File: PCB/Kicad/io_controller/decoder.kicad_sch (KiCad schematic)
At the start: 3 parts, among them U10 74LS08, U11 74LS08, U9 74LS02

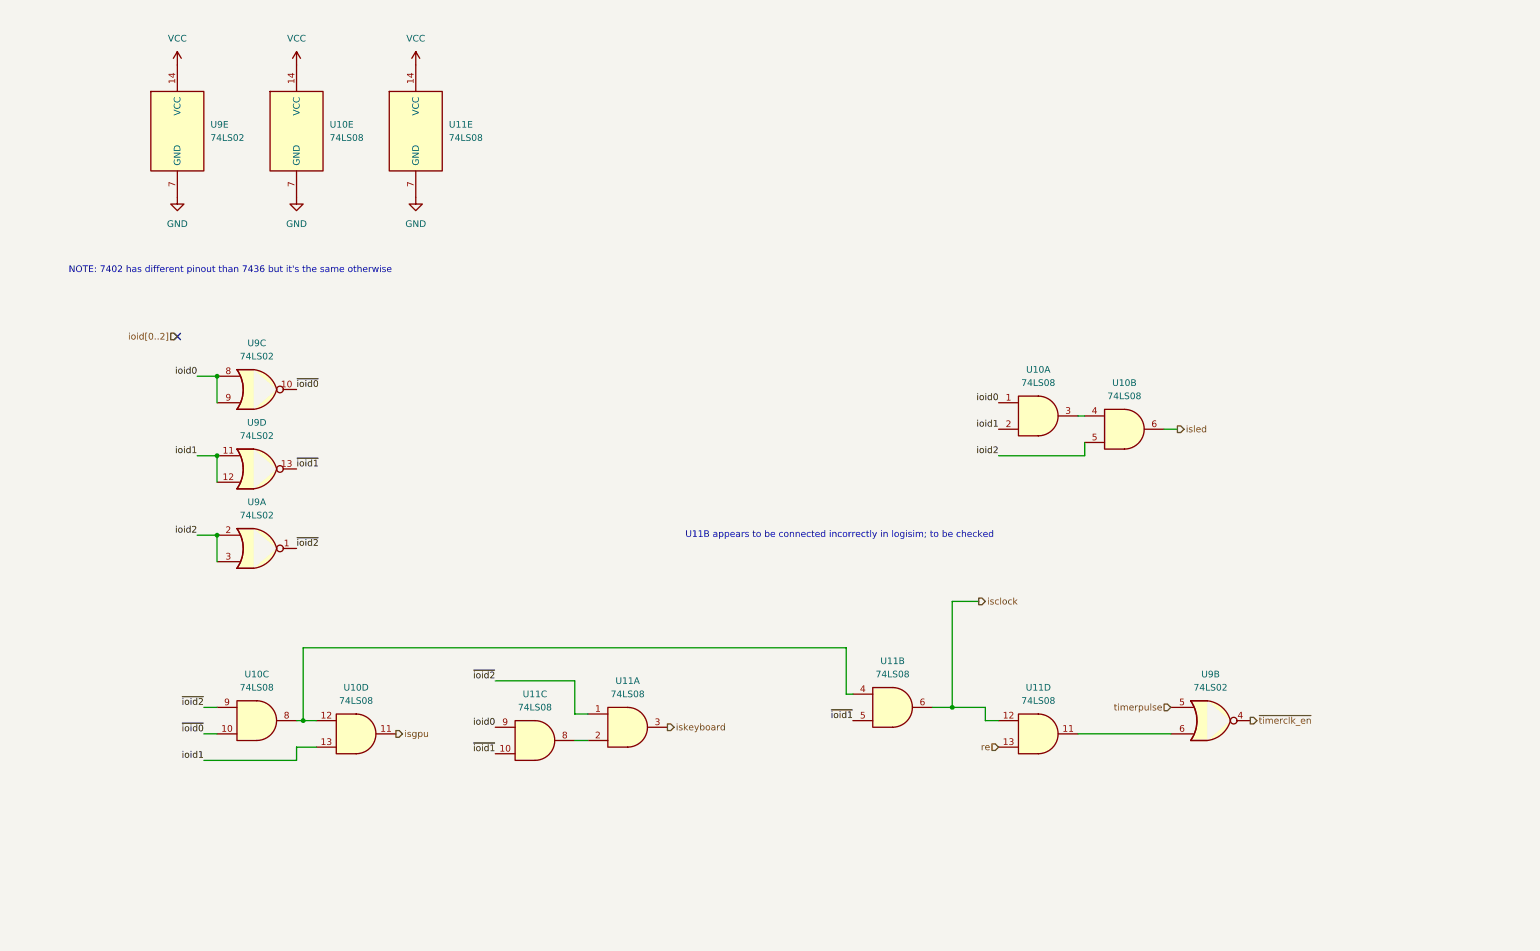
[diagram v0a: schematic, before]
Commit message: initial version of io controller schematic
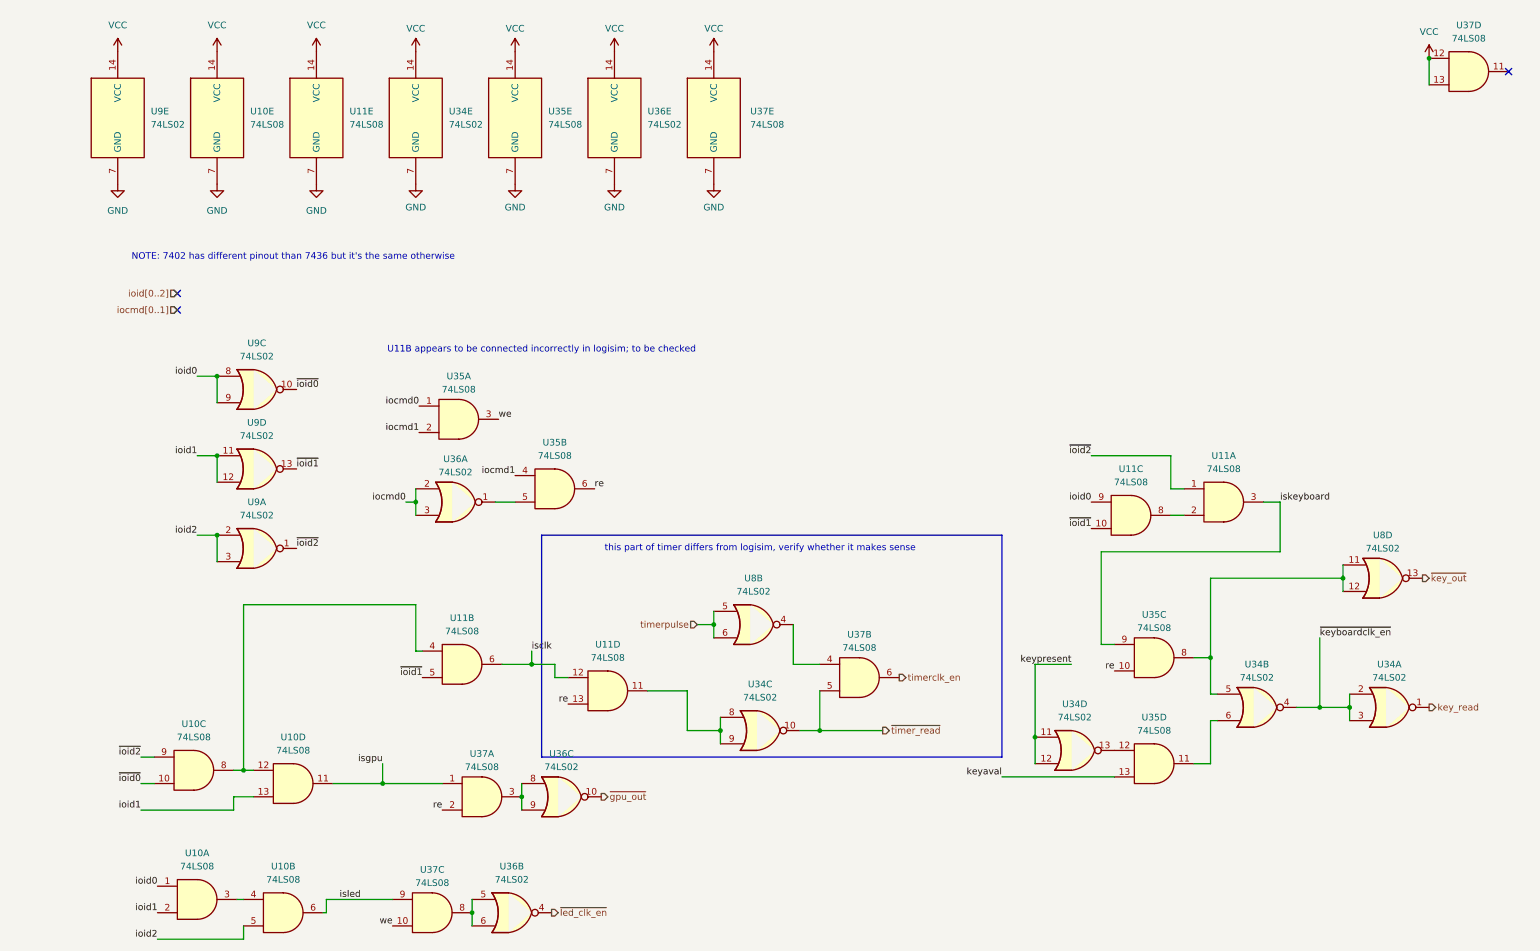
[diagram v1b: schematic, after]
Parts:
- removed unit 2 of U9
- added U34, U36, U8: 74LS02, symbol 74xx:74LS02
- added U35, U37: 74LS08, symbol 74xx:74LS08
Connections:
- net GND: now also U34.7 (GND), U35.7 (GND), U36.7 (GND), U37.7 (GND)
- net VCC: now also U34.14 (VCC), U35.14 (VCC), U36.14 (VCC), U37.12, U37.13, U37.14 (VCC)
- net isgpu: now also U37.1
- net iskeyboard: now also U35.9
- net isled: now also U37.9
- net re: now also U35.10, U35.6, U37.2
- net timerpulse: now also U8.5, U8.6
- net at U11.11: now also U34.8, U34.9
- net isclock renamed isclk
- new net: U37.4, U8.4
- new net: U36.8, U36.9, U37.3
- new net: U35.5, U36.1
- new net: U34.5, U35.8, U8.11, U8.12
- new net: U34.6, U35.11
- new net: U34.13, U35.12
- new net: U36.5, U36.6, U37.8
- new net iocmd0: U35.1, U36.2, U36.3
- new net iocmd1: U35.2, U35.4
- new net key_read: U34.1
- new net keyaval: U35.13
- new net keypresent: U34.11, U34.12
- new net timerclk_en: U37.6
- new net we: U35.3, U37.10
- new net ~{gpu_out}: U36.10
- new net ~{key_out}: U8.13
- new net ~{keyboardclk_en}: U34.2, U34.3, U34.4
- new net ~{led_clk_en}: U36.4
- new net ~{timer_read}: U34.10, U37.5
- no-connect marks 1 -> 3
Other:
- note added: "this part of timer differs from logisim, verify whether it makes sense"
- moved on the sheet: U10A, U10B, U10C, U10D, U10E, U11A, U11B, U11C, U11D, U11E, U9E

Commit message: io controller WIP ; simulated timer ; adjusted decoder ; adjusted LEDs
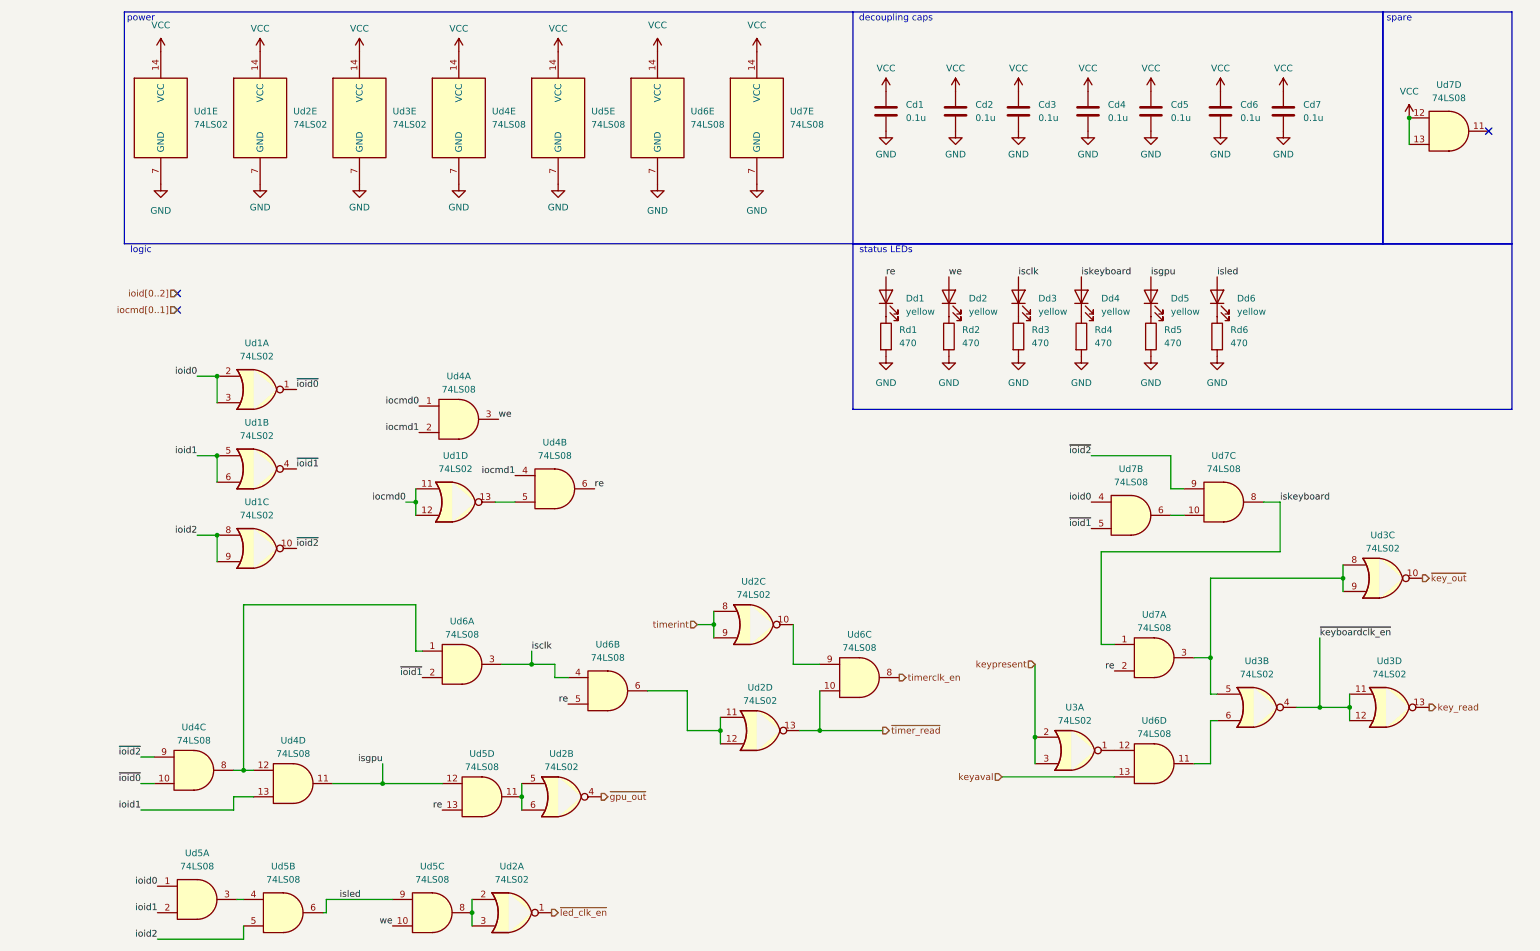
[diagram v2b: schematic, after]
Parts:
- added Cd1, Cd2, Cd3, Cd4, Cd5, Cd6, Cd7: 0.1u, Capacitor_SMD:C_0402_1005Metric, symbol Device:C
- added Dd1, Dd2, Dd3, Dd4, Dd5, Dd6: yellow, LED_SMD:LED_0603_1608Metric, symbol Device:LED
- added Rd1, Rd2, Rd3, Rd4, Rd5, Rd6: 470, Resistor_SMD:R_0402_1005Metric, symbol Device:R
- Ud1: renamed from U9; footprint (none) -> Package_SO:SO-14_3.9x8.65mm_P1.27mm
- Ud1, Ud2, Ud3: renamed from U36; footprint (none) -> Package_SO:SO-14_3.9x8.65mm_P1.27mm
- Ud2, Ud3: renamed from U34; footprint (none) -> Package_SO:SO-14_3.9x8.65mm_P1.27mm
- Ud2, Ud3: renamed from U8; footprint (none) -> Package_SO:SO-14_3.9x8.65mm_P1.27mm
- Ud4, Ud5, Ud6: renamed from U10; footprint (none) -> Package_SO:SOIC-14_3.9x8.7mm_P1.27mm
- Ud4, Ud6, Ud7: renamed from U35; footprint (none) -> Package_SO:SOIC-14_3.9x8.7mm_P1.27mm
- Ud5, Ud6, Ud7: renamed from U37; footprint (none) -> Package_SO:SOIC-14_3.9x8.7mm_P1.27mm
- Ud6, Ud7: renamed from U11; footprint (none) -> Package_SO:SOIC-14_3.9x8.7mm_P1.27mm
- renumbered U34 to U3
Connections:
- net GND: now also Cd1.2, Cd2.2, Cd3.2, Cd4.2, Cd5.2, Cd6.2, Cd7.2, Rd1.2, Rd2.2, Rd3.2, Rd4.2, Rd5.2, Rd6.2
- net VCC: now also Cd1.1, Cd2.1, Cd3.1, Cd4.1, Cd5.1, Cd6.1, Cd7.1
- net iocmd0: now also Ud1.11, Ud1.12; no longer Ud1.2, Ud1.3
- net ioid0: now also Ud1.2, Ud1.3, Ud7.4; no longer Ud1.8, Ud1.9, Ud7.9
- net ioid1: now also Ud1.5, Ud1.6; no longer Ud1.11, Ud1.12
- net ioid2: now also Ud1.8, Ud1.9; no longer Ud1.2, Ud1.3
- net isclk: now also Ud6.3, Ud6.4, Dd3.2 (A); no longer Ud6.12, Ud6.6
- net isgpu: now also Ud5.12, Dd5.2 (A); no longer Ud5.1
- net iskeyboard: now also Ud7.1, Ud7.8, Dd4.2 (A); no longer Ud7.3, Ud7.9
- net isled: now also Dd6.2 (A)
- net key_read: now also Ud3.13; no longer Ud3.1
- net keypresent: now also U3.2, U3.3; no longer U3.11, U3.12
- net re: now also Ud5.13, Ud6.5, Ud7.2, Dd1.2 (A); no longer Ud5.2, Ud6.13, Ud7.10
- net timerclk_en: now also Ud6.8; no longer Ud6.6
- net we: now also Dd2.2 (A)
- net ~{gpu_out}: now also Ud2.4; no longer Ud2.10
- net ~{ioid0}: now also Ud1.1; no longer Ud1.10
- net ~{ioid1}: now also Ud1.4, Ud6.2, Ud7.5; no longer Ud1.13, Ud6.5, Ud7.10
- net ~{ioid2}: now also Ud1.10, Ud7.9; no longer Ud1.1, Ud7.1
- net ~{key_out}: now also Ud3.10; no longer Ud3.13
- net ~{keyboardclk_en}: now also Ud3.11, Ud3.12; no longer Ud3.2, Ud3.3
- net ~{led_clk_en}: now also Ud2.1; no longer Ud2.4
- net ~{timer_read}: now also Ud2.13, Ud6.10; no longer Ud2.10, Ud6.5
- net at Ud4.12, Ud4.8: now also Ud6.1; no longer Ud6.4
- net at Ud4.5: now also Ud1.13; no longer Ud1.1
- net at Ud6.12: now also U3.1; no longer U3.13
- removed net timerpulse: Ud2.5, Ud2.6
- new net: Ud2.10, Ud6.9
- new net: Dd3.1 (K), Rd3.1
- new net: Ud2.5, Ud2.6, Ud5.11
- new net: Ud2.11, Ud2.12, Ud6.6
- new net: Dd2.1 (K), Rd2.1
- new net: Dd5.1 (K), Rd5.1
- new net: Ud3.5, Ud3.8, Ud3.9, Ud7.3
- new net: Ud7.10, Ud7.6
- new net: Dd6.1 (K), Rd6.1
- new net: Ud2.2, Ud2.3, Ud5.8
- new net: Dd4.1 (K), Rd4.1
- new net: Dd1.1 (K), Rd1.1
- new net timerint: Ud2.8, Ud2.9
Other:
- note added: "decoupling caps"
- note added: "logic"
- note added: "power"
- note added: "spare"
- note added: "status LEDs"
- note removed: "NOTE: 7402 has different pinout than 7436 but it's the same otherwise"
- note removed: "U11B appears to be connected incorrectly in logisim; to be checked"
- note removed: "this part of timer differs from logisim, verify whether it makes sense"
- company: (none) -> AGH Logic Unit
- title: (none) -> Decoder
- moved on the sheet: Ud1E, Ud2E, Ud3E, Ud4E, Ud5E, Ud6E, Ud7D, Ud7E

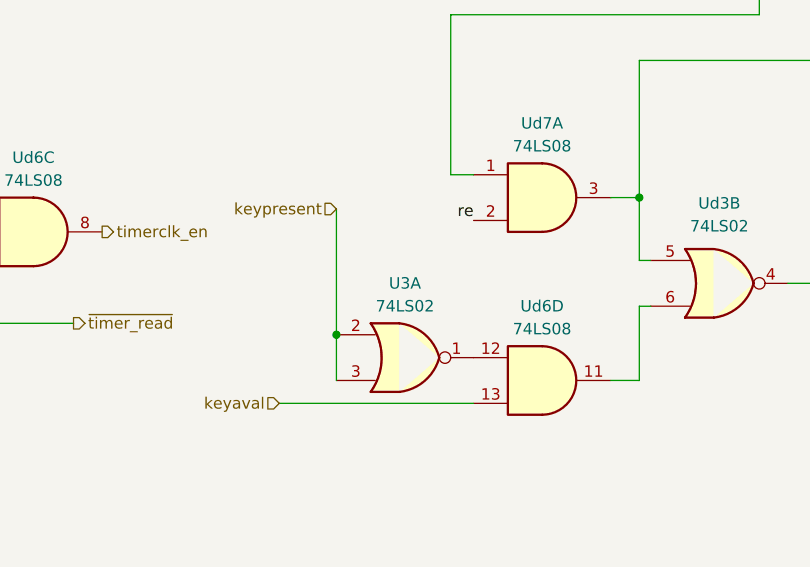
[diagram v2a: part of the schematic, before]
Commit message: more spice models and bugfixes ; more tests of io_controller - mostly keyboard
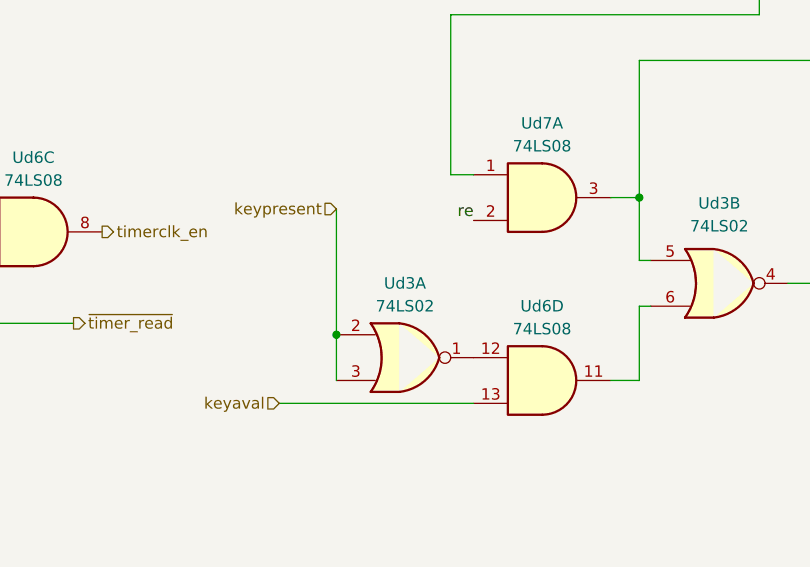
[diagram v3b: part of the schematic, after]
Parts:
- renumbered U3 to Ud3
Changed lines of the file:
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@@
 		(dnp no)
 		(fields_autoplaced yes)
-		(property "Reference" "U3"
+		(property "Reference" "Ud3"
 			(at 201.295 146.05 0)
 			(effects
@@
 			(project "io_controller"
 				(path "/dccec861-b967-466c-843e-d6d1ad6064ce/7889a309-dbe1-4a3b-a691-b2c761732dff"
-					(reference "U3")
+					(reference "Ud3")
 					(unit 1)
 				)

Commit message: primarily keyboard decoder finish ; preliminary layout
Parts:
- Ud3: footprint (none) -> Package_SO:SO-14_3.9x8.65mm_P1.27mm
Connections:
- net keypresent is gone; now on net key_read: Ud3.2, Ud3.3
- net VCC: now also Ud3.11, Ud3.12, Ud3.5, Ud3.6, Ud3.8, Ud3.9
- net iskeyboard: now also Ud6.12; no longer Ud7.1
- net key_read: now also Ud6.11; no longer Ud3.13
- net ~{key_out}: now also Ud3.1; no longer Ud3.10
- net keyaval: no longer names the net of Ud6.13
- net keyaval: now also Ud7.3
- removed net ~{keyboardclk_en}: Ud3.11, Ud3.12, Ud3.4
- new net keyready: Ud7.1
- no-connect marks 3 -> 6
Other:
- moved on the sheet: Ud3A, Ud3B, Ud3C, Ud3D, Ud6D, Ud7D
